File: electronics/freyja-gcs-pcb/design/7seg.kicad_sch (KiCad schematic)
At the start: 22 parts, among them Q10 AO4459, Q9 AO4459, U10 74HC595, U3 74HC595

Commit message: global reset
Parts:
- removed R52: 100k, symbol Device:R
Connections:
- net NRST: now reaches U3.10 (~{SRCLR})
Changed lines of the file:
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@@
 	)
 	(junction
-		(at 163.83 71.12)
-		(diameter 0)
-		(color 0 0 0 0)
-	)
-	(junction
 		(at 138.43 124.46)
 		(diameter 0)
@@
 	(wire
 		(pts
-			(xy 154.94 71.12) (xy 144.78 71.12)
-		)
-		(stroke
-			(width 0)
-			(type default)
-		)
-	)
-	(wire
-		(pts
 			(xy 90.17 92.71) (xy 90.17 107.95)
 		)
@@
 	(wire
 		(pts
-			(xy 163.83 71.12) (xy 163.83 82.55)
-		)
-		(stroke
-			(width 0)
-			(type default)
-		)
-	)
-	(wire
-		(pts
 			(xy 200.66 100.33) (xy 200.66 101.6)
 		)
@@
 	(wire
 		(pts
-			(xy 163.83 60.96) (xy 163.83 71.12)
+			(xy 163.83 60.96) (xy 163.83 82.55)
 		)
 		(stroke
@@
 	(wire
 		(pts
-			(xy 163.83 71.12) (xy 162.56 71.12)
-		)
-		(stroke
-			(width 0)
-			(type default)
-		)
-	)
-	(wire
-		(pts
 			(xy 135.89 127) (xy 167.64 127)
 		)
@@
 	(wire
 		(pts
-			(xy 144.78 71.12) (xy 144.78 72.39)
+			(xy 144.78 58.42) (xy 144.78 72.39)
 		)
 		(stroke
@@
 		)
 	)
+	(global_label "NRST"
+		(shape input)
+		(at 144.78 58.42 90)
+		(fields_autoplaced yes)
+		(effects
+			(font
+				(size 1.27 1.27)
+			)
+			(justify left)
+		)
+		(property "Intersheetrefs" "${INTERSHEET_REFS}"
+			(at 144.78 50.6572 90)
+			(effects
+				(font
+					(size 1.27 1.27)
+				)
+				(justify left)
+				(hide yes)
+			)
+		)
+	)
 	(global_label "7SEG_DA"
 		(shape input)
@@
 					(unit 1)
 				)
-			)
-		)
-	)
-	(symbol
-		(lib_id "Device:R")
-		(at 158.75 71.12 90)
-		(mirror x)
-		(unit 1)
-		(exclude_from_sim no)
-		(in_bom yes)
-		(on_board yes)
-		(dnp no)
-		(property "Reference" "R52"
-			(at 160.0201 68.58 0)
-			(effects
-				(font
-					(size 1.27 1.27)
-				)
-				(justify right)
-			)
-		)
-		(property "Value" "100k"
-			(at 157.4801 68.58 0)
-			(effects
-				(font
-					(size 1.27 1.27)
-				)
-				(justify right)
-			)
-		)
-		(property "Footprint" ""
-			(at 158.75 69.342 90)
-			(effects
-				(font
-					(size 1.27 1.27)
-				)
-				(hide yes)
-			)
-		)
-		(property "Datasheet" "~"
-			(at 158.75 71.12 0)
-			(effects
-				(font
-					(size 1.27 1.27)
-				)
-				(hide yes)
-			)
-		)
-		(property "Description" "Resistor"
-			(at 158.75 71.12 0)
-			(effects
-				(font
-					(size 1.27 1.27)
-				)
-				(hide yes)
-			)
-		)
-		(pin "2"
-		)
-		(pin "1"
-		)
-		(instances
-			(project "freyja-gcs-pcb"
-				(path "/c292fa04-82ad-49e9-a9d8-422554d1d11d/824ebaf0-8cb2-47d2-898f-7e11886db031"
-					(reference "R52")
-					(unit 1)
-				)

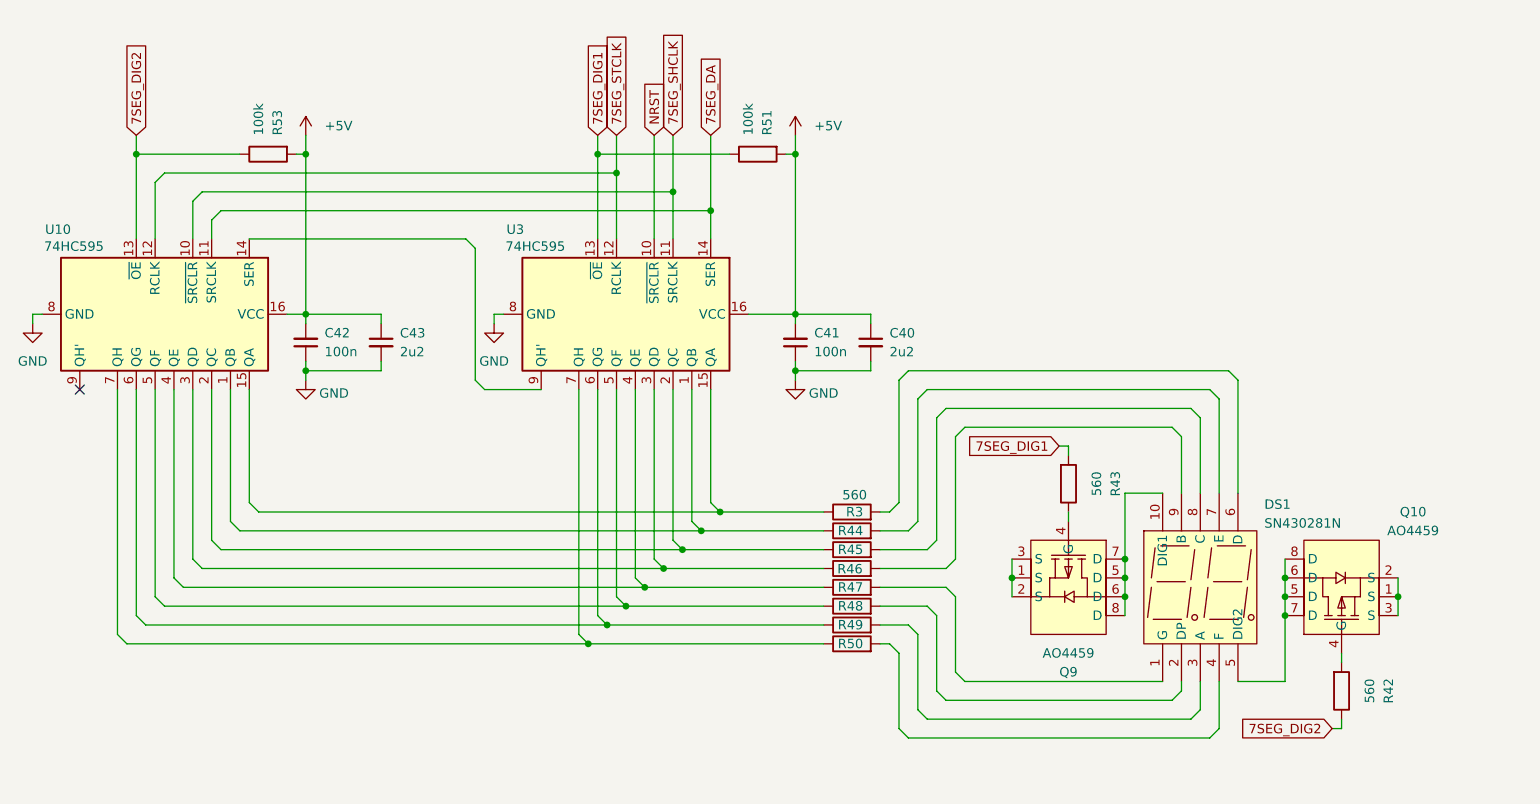
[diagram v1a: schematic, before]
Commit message: reset designators
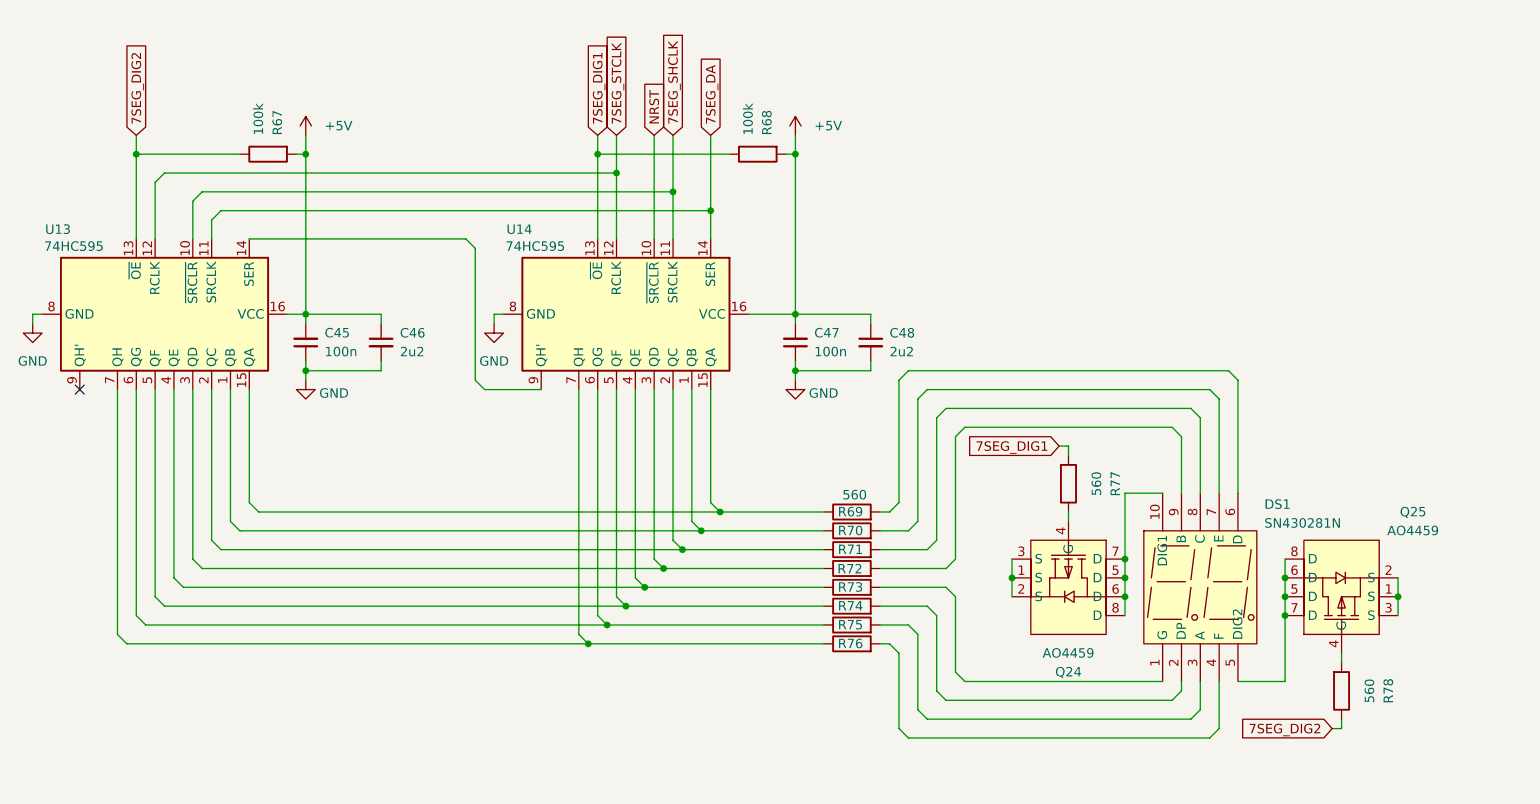
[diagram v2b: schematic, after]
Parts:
- renumbered C42 to C45, C43 to C46, C41 to C47, C40 to C48, Q9 to Q24, Q10 to Q25, R53 to R67, R51 to R68, R3 to R69, R44 to R70, R45 to R71, R46 to R72, R47 to R73, R48 to R74, R49 to R75, R50 to R76, R43 to R77, R42 to R78, U10 to U13, U3 to U14
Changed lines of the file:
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@@
 		(on_board yes)
 		(dnp no)
-		(property "Reference" "R47"
+		(property "Reference" "R73"
 			(at 172.974 119.38 90)
 			(effects
@@
 			(project "freyja-gcs-pcb"
 				(path "/c292fa04-82ad-49e9-a9d8-422554d1d11d/824ebaf0-8cb2-47d2-898f-7e11886db031"
-					(reference "R47")
+					(reference "R73")
 					(unit 1)
 				)
@@
 		(on_board yes)
 		(dnp no)
-		(property "Reference" "#PWR061"
+		(property "Reference" "#PWR0117"
 			(at 163.83 97.79 0)
 			(effects
@@
 			(project "freyja-gcs-pcb"
 				(path "/c292fa04-82ad-49e9-a9d8-422554d1d11d/824ebaf0-8cb2-47d2-898f-7e11886db031"
-					(reference "#PWR061")
+					(reference "#PWR0117")
 					(unit 1)
 				)
@@
 		(dnp no)
 		(fields_autoplaced yes)
-		(property "Reference" "#PWR013"
+		(property "Reference" "#PWR0116"
 			(at 163.83 62.23 0)
 			(effects
@@
 			(project "freyja-gcs-pcb"
 				(path "/c292fa04-82ad-49e9-a9d8-422554d1d11d/824ebaf0-8cb2-47d2-898f-7e11886db031"
-					(reference "#PWR013")
+					(reference "#PWR0116")
 					(unit 1)
 				)
@@
 		(on_board yes)
 		(dnp no)
-		(property "Reference" "C43"
+		(property "Reference" "C46"
 			(at 110.49 85.0962 0)
 			(effects
@@
 			(project "freyja-gcs-pcb"
 				(path "/c292fa04-82ad-49e9-a9d8-422554d1d11d/824ebaf0-8cb2-47d2-898f-7e11886db031"
-					(reference "C43")
+					(reference "C46")
 					(unit 1)
 				)
@@
 		(dnp no)
 		(fields_autoplaced yes)
-		(property "Reference" "#PWR079"
+		(property "Reference" "#PWR0115"
 			(at 123.19 90.17 0)
 			(effects
@@
 			(project ""
 				(path "/c292fa04-82ad-49e9-a9d8-422554d1d11d/824ebaf0-8cb2-47d2-898f-7e11886db031"
-					(reference "#PWR079")
+					(reference "#PWR0115")
 					(unit 1)
 				)
@@
 		(on_board yes)
 		(dnp no)
-		(property "Reference" "R53"
+		(property "Reference" "R67"
 			(at 93.9801 58.42 0)
 			(effects
@@
 			(project "freyja-gcs-pcb"
 				(path "/c292fa04-82ad-49e9-a9d8-422554d1d11d/824ebaf0-8cb2-47d2-898f-7e11886db031"
-					(reference "R53")
+					(reference "R67")
 					(unit 1)
 				)
@@
 		(on_board yes)
 		(dnp no)
-		(property "Reference" "R49"
+		(property "Reference" "R75"
 			(at 172.974 124.46 90)
 			(effects
@@
 			(project "freyja-gcs-pcb"
 				(path "/c292fa04-82ad-49e9-a9d8-422554d1d11d/824ebaf0-8cb2-47d2-898f-7e11886db031"
-					(reference "R49")
+					(reference "R75")
 					(unit 1)
 				)
@@
 		(on_board yes)
 		(dnp no)
-		(property "Reference" "#PWR082"
+		(property "Reference" "#PWR0114"
 			(at 97.79 97.79 0)
 			(effects
@@
 			(project "freyja-gcs-pcb"
 				(path "/c292fa04-82ad-49e9-a9d8-422554d1d11d/824ebaf0-8cb2-47d2-898f-7e11886db031"
-					(reference "#PWR082")
+					(reference "#PWR0114")
 					(unit 1)
 				)
@@
 		(on_board yes)
 		(dnp no)
-		(property "Reference" "C40"
+		(property "Reference" "C48"
 			(at 176.53 85.0962 0)
 			(effects
@@
 			(project "freyja-gcs-pcb"
 				(path "/c292fa04-82ad-49e9-a9d8-422554d1d11d/824ebaf0-8cb2-47d2-898f-7e11886db031"
-					(reference "C40")
+					(reference "C48")
 					(unit 1)
 				)
@@
 		(on_board yes)
 		(dnp no)
-		(property "Reference" "U3"
+		(property "Reference" "U14"
 			(at 124.8567 71.12 90)
 			(effects
@@
 			(project "freyja-gcs-pcb"
 				(path "/c292fa04-82ad-49e9-a9d8-422554d1d11d/824ebaf0-8cb2-47d2-898f-7e11886db031"
-					(reference "U3")
+					(reference "U14")
 					(unit 1)
 				)
@@
 		(on_board yes)
 		(dnp no)
-		(property "Reference" "R51"
+		(property "Reference" "R68"
 			(at 160.0201 58.42 0)
 			(effects
@@
 			(project "freyja-gcs-pcb"
 				(path "/c292fa04-82ad-49e9-a9d8-422554d1d11d/824ebaf0-8cb2-47d2-898f-7e11886db031"
-					(reference "R51")
+					(reference "R68")
 					(unit 1)
 				)
@@
 		(on_board yes)
 		(dnp no)
-		(property "Reference" "U10"
+		(property "Reference" "U13"
 			(at 62.6267 71.12 90)
 			(effects
@@
 			(project "freyja-gcs-pcb"
 				(path "/c292fa04-82ad-49e9-a9d8-422554d1d11d/824ebaf0-8cb2-47d2-898f-7e11886db031"
-					(reference "U10")
+					(reference "U13")
 					(unit 1)
 				)
@@
 		(on_board yes)
 		(dnp no)
-		(property "Reference" "Q9"
+		(property "Reference" "Q24"
 			(at 200.66 130.81 90)
 			(effects
@@
 			(project "freyja-gcs-pcb"
 				(path "/c292fa04-82ad-49e9-a9d8-422554d1d11d/824ebaf0-8cb2-47d2-898f-7e11886db031"
-					(reference "Q9")
+					(reference "Q24")
 					(unit 1)
 				)
@@
 		(on_board yes)
 		(dnp no)
-		(property "Reference" "R42"
+		(property "Reference" "R78"
 			(at 243.84 133.35 90)
 			(effects
@@
 			(project "freyja-gcs-pcb"
 				(path "/c292fa04-82ad-49e9-a9d8-422554d1d11d/824ebaf0-8cb2-47d2-898f-7e11886db031"
-					(reference "R42")
+					(reference "R78")
 					(unit 1)
 				)
@@
 		(dnp no)
 		(fields_autoplaced yes)
-		(property "Reference" "#PWR080"
+		(property "Reference" "#PWR0113"
 			(at 97.79 62.23 0)
 			(effects
@@
 			(project "freyja-gcs-pcb"
 				(path "/c292fa04-82ad-49e9-a9d8-422554d1d11d/824ebaf0-8cb2-47d2-898f-7e11886db031"
-					(reference "#PWR080")
+					(reference "#PWR0113")
 					(unit 1)
 				)
@@
 		(on_board yes)
 		(dnp no)
-		(property "Reference" "R3"
+		(property "Reference" "R69"
 			(at 172.974 109.22 90)
 			(effects
@@
 			(project "freyja-gcs-pcb"
 				(path "/c292fa04-82ad-49e9-a9d8-422554d1d11d/824ebaf0-8cb2-47d2-898f-7e11886db031"
-					(reference "R3")
+					(reference "R69")
 					(unit 1)
 				)
@@
 		(on_board yes)
 		(dnp no)
-		(property "Reference" "R48"
+		(property "Reference" "R74"
 			(at 172.974 121.92 90)
 			(effects
@@
 			(project "freyja-gcs-pcb"
 				(path "/c292fa04-82ad-49e9-a9d8-422554d1d11d/824ebaf0-8cb2-47d2-898f-7e11886db031"
-					(reference "R48")
+					(reference "R74")
 					(unit 1)
 				)
@@
 		(dnp no)
 		(fields_autoplaced yes)
-		(property "Reference" "#PWR081"
+		(property "Reference" "#PWR0112"
 			(at 60.96 90.17 0)
 			(effects
@@
 			(project "freyja-gcs-pcb"
 				(path "/c292fa04-82ad-49e9-a9d8-422554d1d11d/824ebaf0-8cb2-47d2-898f-7e11886db031"
-					(reference "#PWR081")
+					(reference "#PWR0112")
 					(unit 1)
 				)
@@
 		(on_board yes)
 		(dnp no)
-		(property "Reference" "R50"
+		(property "Reference" "R76"
 			(at 172.974 127 90)
 			(effects
@@
 			(project "freyja-gcs-pcb"
 				(path "/c292fa04-82ad-49e9-a9d8-422554d1d11d/824ebaf0-8cb2-47d2-898f-7e11886db031"
-					(reference "R50")
+					(reference "R76")
 					(unit 1)
 				)
@@
 		(on_board yes)
 		(dnp no)
-		(property "Reference" "R46"
+		(property "Reference" "R72"
 			(at 172.9042 116.9175 90)
 			(effects
@@
 			(project "freyja-gcs-pcb"
 				(path "/c292fa04-82ad-49e9-a9d8-422554d1d11d/824ebaf0-8cb2-47d2-898f-7e11886db031"
-					(reference "R46")
+					(reference "R72")
 					(unit 1)
 				)
@@
 		(dnp no)
 		(fields_autoplaced yes)
-		(property "Reference" "C42"
+		(property "Reference" "C45"
 			(at 100.33 85.0835 0)
 			(effects
@@
 			(project "freyja-gcs-pcb"
 				(path "/c292fa04-82ad-49e9-a9d8-422554d1d11d/824ebaf0-8cb2-47d2-898f-7e11886db031"
-					(reference "C42")
+					(reference "C45")
 					(unit 1)
 				)
@@
 		(on_board yes)
 		(dnp no)
-		(property "Reference" "Q10"
+		(property "Reference" "Q25"
 			(at 247.142 109.22 90)
 			(effects
@@
 			(project "freyja-gcs-pcb"
 				(path "/c292fa04-82ad-49e9-a9d8-422554d1d11d/824ebaf0-8cb2-47d2-898f-7e11886db031"
-					(reference "Q10")
+					(reference "Q25")
 					(unit 1)
 				)
@@
 		(on_board yes)
 		(dnp no)
-		(property "Reference" "R45"
+		(property "Reference" "R71"
 			(at 172.974 114.3 90)
 			(effects
@@
 			(project "freyja-gcs-pcb"
 				(path "/c292fa04-82ad-49e9-a9d8-422554d1d11d/824ebaf0-8cb2-47d2-898f-7e11886db031"
-					(reference "R45")
+					(reference "R71")
 					(unit 1)
 				)
@@
 		(on_board yes)
 		(dnp no)
-		(property "Reference" "R44"
+		(property "Reference" "R70"
 			(at 172.974 111.76 90)
 			(effects
@@
 			(project "freyja-gcs-pcb"
 				(path "/c292fa04-82ad-49e9-a9d8-422554d1d11d/824ebaf0-8cb2-47d2-898f-7e11886db031"
-					(reference "R44")
+					(reference "R70")
 					(unit 1)
 				)
@@
 		(dnp no)
 		(fields_autoplaced yes)
-		(property "Reference" "C41"
+		(property "Reference" "C47"
 			(at 166.37 85.0835 0)
 			(effects
@@
 			(project "freyja-gcs-pcb"
 				(path "/c292fa04-82ad-49e9-a9d8-422554d1d11d/824ebaf0-8cb2-47d2-898f-7e11886db031"
-					(reference "C41")
+					(reference "C47")
 					(unit 1)
 				)
@@
 		(on_board yes)
 		(dnp no)
-		(property "Reference" "R43"
+		(property "Reference" "R77"
 			(at 207.01 105.41 90)
 			(effects
@@
 			(project "freyja-gcs-pcb"
 				(path "/c292fa04-82ad-49e9-a9d8-422554d1d11d/824ebaf0-8cb2-47d2-898f-7e11886db031"
-					(reference "R43")
-					(unit 1)
-				)
+					(reference "R77")
+					(unit 1)
+				)

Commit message: footprint and lcsc part for all components
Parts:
- C45, C47: footprint (none) -> Capacitor_SMD:C_0603_1608Metric; LCSC Part (none) -> C2762593
- C46, C48: footprint (none) -> Capacitor_SMD:C_0603_1608Metric; LCSC Part (none) -> C913904
- R67, R68: footprint (none) -> Resistor_SMD:R_0603_1608Metric; LCSC Part (none) -> C25803
- R69, R70, R71, R72, R73, R74, R75, R76, R77, R78: footprint (none) -> Resistor_SMD:R_0603_1608Metric; LCSC Part (none) -> C23204
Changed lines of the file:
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@@
 			)
 		)
-		(property "Footprint" ""
+		(property "Footprint" "Resistor_SMD:R_0603_1608Metric"
 			(at 171.45 121.158 90)
 			(effects
@@
 		(property "Description" "Resistor"
 			(at 171.45 119.38 0)
+			(effects
+				(font
+					(size 1.27 1.27)
+				)
+				(hide yes)
+			)
+		)
+		(property "LCSC Part" "C23204"
+			(at 171.45 119.38 90)
 			(effects
 				(font
@@
 			)
 		)
-		(property "Footprint" ""
+		(property "Footprint" "Capacitor_SMD:C_0603_1608Metric"
 			(at 107.95 86.36 0)
 			(effects
@@
 		)
 		(property "Description" "Unpolarized capacitor, small symbol"
+			(at 107.95 86.36 0)
+			(effects
+				(font
+					(size 1.27 1.27)
+				)
+				(hide yes)
+			)
+		)
+		(property "LCSC Part" "C913904"
 			(at 107.95 86.36 0)
 			(effects
@@
 			)
 		)
-		(property "Footprint" ""
+		(property "Footprint" "Resistor_SMD:R_0603_1608Metric"
 			(at 92.71 59.182 90)
 			(effects
@@
 			)
 		)
+		(property "LCSC Part" "C25803"
+			(at 92.71 60.96 0)
+			(effects
+				(font
+					(size 1.27 1.27)
+				)
+				(hide yes)
+			)
+		)
 		(pin "2"
 		)
@@
 			)
 		)
-		(property "Footprint" ""
+		(property "Footprint" "Resistor_SMD:R_0603_1608Metric"
 			(at 171.45 126.238 90)
 			(effects
@@
 		(property "Description" "Resistor"
 			(at 171.45 124.46 0)
+			(effects
+				(font
+					(size 1.27 1.27)
+				)
+				(hide yes)
+			)
+		)
+		(property "LCSC Part" "C23204"
+			(at 171.45 124.46 90)
 			(effects
 				(font
@@
 			)
 		)
-		(property "Footprint" ""
+		(property "Footprint" "Capacitor_SMD:C_0603_1608Metric"
 			(at 173.99 86.36 0)
 			(effects
@@
 		)
 		(property "Description" "Unpolarized capacitor, small symbol"
+			(at 173.99 86.36 0)
+			(effects
+				(font
+					(size 1.27 1.27)
+				)
+				(hide yes)
+			)
+		)
+		(property "LCSC Part" "C913904"
 			(at 173.99 86.36 0)
 			(effects
@@
 			)
 		)
-		(property "Footprint" ""
+		(property "Footprint" "Resistor_SMD:R_0603_1608Metric"
 			(at 158.75 59.182 90)
 			(effects
@@
 		)
 		(property "Description" "Resistor"
+			(at 158.75 60.96 0)
+			(effects
+				(font
+					(size 1.27 1.27)
+				)
+				(hide yes)
+			)
+		)
+		(property "LCSC Part" "C25803"
 			(at 158.75 60.96 0)
 			(effects
@@
 			)
 		)
-		(property "Footprint" ""
+		(property "Footprint" "Resistor_SMD:R_0603_1608Metric"
 			(at 235.712 133.35 90)
 			(effects
@@
 		(property "Description" "Resistor"
 			(at 237.49 133.35 0)
+			(effects
+				(font
+					(size 1.27 1.27)
+				)
+				(hide yes)
+			)
+		)
+		(property "LCSC Part" "C23204"
+			(at 237.49 133.35 90)
 			(effects
 				(font
@@
 			)
 		)
-		(property "Footprint" ""
+		(property "Footprint" "Resistor_SMD:R_0603_1608Metric"
 			(at 171.45 110.998 90)
 			(effects
@@
 			)
 		)
+		(property "LCSC Part" "C23204"
+			(at 171.45 109.22 90)
+			(effects
+				(font
+					(size 1.27 1.27)
+				)
+				(hide yes)
+			)
+		)
 		(pin "1"
 		)
@@
 			)
 		)
-		(property "Footprint" ""
+		(property "Footprint" "Resistor_SMD:R_0603_1608Metric"
 			(at 171.45 123.698 90)
 			(effects
@@
 		(property "Description" "Resistor"
 			(at 171.45 121.92 0)
+			(effects
+				(font
+					(size 1.27 1.27)
+				)
+				(hide yes)
+			)
+		)
+		(property "LCSC Part" "C23204"
+			(at 171.45 121.92 90)
 			(effects
 				(font
@@
 			)
 		)
-		(property "Footprint" ""
+		(property "Footprint" "Resistor_SMD:R_0603_1608Metric"
 			(at 171.45 128.778 90)
 			(effects
@@
 			)
 		)
+		(property "LCSC Part" "C23204"
+			(at 171.45 127 90)
+			(effects
+				(font
+					(size 1.27 1.27)
+				)
+				(hide yes)
+			)
+		)
 		(pin "1"
 		)
@@
 			)
 		)
-		(property "Footprint" ""
+		(property "Footprint" "Resistor_SMD:R_0603_1608Metric"
 			(at 171.45 118.618 90)
 			(effects
@@
 		(property "Description" "Resistor"
 			(at 171.45 116.84 0)
+			(effects
+				(font
+					(size 1.27 1.27)
+				)
+				(hide yes)
+			)
+		)
+		(property "LCSC Part" "C23204"
+			(at 171.45 116.84 90)
 			(effects
 				(font
@@
 			)
 		)
-		(property "Footprint" ""
+		(property "Footprint" "Capacitor_SMD:C_0603_1608Metric"
 			(at 97.79 86.36 0)
 			(effects
@@
 			)
 		)
+		(property "LCSC Part" "C2762593"
+			(at 97.79 86.36 0)
+			(effects
+				(font
+					(size 1.27 1.27)
+				)
+				(hide yes)
+			)
+		)
 		(pin "1"
 		)
@@
 			)
 		)
-		(property "Footprint" ""
+		(property "Footprint" "Resistor_SMD:R_0603_1608Metric"
 			(at 171.45 116.078 90)
 			(effects
@@
 			)
 		)
+		(property "LCSC Part" "C23204"
+			(at 171.45 114.3 90)
+			(effects
+				(font
+					(size 1.27 1.27)
+				)
+				(hide yes)
+			)
+		)
 		(pin "1"
 		)
@@
 			)
 		)
-		(property "Footprint" ""
+		(property "Footprint" "Resistor_SMD:R_0603_1608Metric"
 			(at 171.45 113.538 90)
 			(effects
@@
 		(property "Description" "Resistor"
 			(at 171.45 111.76 0)
+			(effects
+				(font
+					(size 1.27 1.27)
+				)
+				(hide yes)
+			)
+		)
+		(property "LCSC Part" "C23204"
+			(at 171.45 111.76 90)
 			(effects
 				(font
@@
 			)
 		)
-		(property "Footprint" ""
+		(property "Footprint" "Capacitor_SMD:C_0603_1608Metric"
 			(at 163.83 86.36 0)
 			(effects
@@
 		)
 		(property "Description" "Unpolarized capacitor, small symbol"
+			(at 163.83 86.36 0)
+			(effects
+				(font
+					(size 1.27 1.27)
+				)
+				(hide yes)
+			)
+		)
+		(property "LCSC Part" "C2762593"
 			(at 163.83 86.36 0)
 			(effects
@@
 			)
 		)
-		(property "Footprint" ""
+		(property "Footprint" "Resistor_SMD:R_0603_1608Metric"
 			(at 198.882 105.41 90)
 			(effects
@@
 			(effects
 				(font
+					(size 1.27 1.27)
+				)
+				(hide yes)
+			)
+		)
+		(property "LCSC Part" "C23204"
+			(at 200.66 105.41 90)
+			(effects
+				(font
